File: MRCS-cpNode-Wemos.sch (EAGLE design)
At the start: 40 parts, among them CON1 3.5MM, CON2 3.5MM, J2 CONNECTOR-GROVE-4P-2.0-347013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, Q2 2n7002, Q3 2n7002, Q4 2n7002, Q5 2n7002, U3 NE555P, U4 MAX3465CPD

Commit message: 5.0
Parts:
- removed C4: 0.1uF, SPCoast:CC0805
- removed C6: .01uF, SPCoast:CC0805
- removed C7: .1uF, SPCoast:CC0805
- removed C8: .1uF, SPCoast:CC0603
- removed CON1, CON2: 3.5MM, SPCoast:CONNECTOR-M035MM-LOCK
- removed CON3, CON4: (no value), SPCoast:CONNECTOR-M025MM-LOCK
- removed D1: BAV-199, SPCoast:DIODE-BAV199
- removed R14: 1k0, SPCoast:R0805-RES
- removed RS485IN: (no value), SparkFun:M05PTH
- removed RS485OUT: (no value), SparkFun:M05LOCK
- removed TX: TX, SPCoast:LED0603-LED
- removed U3: NE555P, SparkFun:NE555P
- removed U4: MAX3465CPD, maxim:MAX3465CPD
- added CMRI-IO: (no value), SPCoast:CONNECTOR-M05LOCK_LONGPADS
- added Q1: 2n7002, SPCoast:MOSFET-N-BSS138-SOT23
- added R4: 10k, SPCoast:R0805-RES
- BOARD: device SPCoast:BOARD69X100 -> SPCoast:BOARD69X90
- R1: value (none) -> 10k; device SPCoast:RPTH-1/6W -> SPCoast:R0805-RES
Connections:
- removed net IN+: CON3.B, CON4.B, RS485IN.1, RS485OUT.1, U4.A
- removed net IN-: CON3.A, CON4.A, RS485IN.2, RS485OUT.2, U4.B
- removed net N$1: C4.1, D1.A, D1.AC, R1.1, U3.DIS, U3.TRE
- removed net N$29: R14.2, TX.A
- removed net N$38: C6.1, U3.CON
- removed net OUT+: CON1.3, CON2.3, RS485IN.3, RS485OUT.3, U4.Y
- removed net OUT-: CON1.2, CON2.2, RS485IN.4, RS485OUT.4, U4.Z
- removed net SHIELD: CON1.1, CON2.1, RS485IN.5, RS485OUT.5
- new net VCC: CMRI-IO.2
- net +3V3: now also Q1.G, R1.2
- net D5: now also Q1.S, R1.1
- net GND: now also CMRI-IO.1; no longer C4.2, C6.2, C7.2, C8.2, TX.C, U3.GND, U4.GND, U4.GND@1
- net RXH: now also CMRI-IO.4; no longer U4.RO
- net TXEN: now also CMRI-IO.5, Q1.D, R4.1; no longer R14.1, U3.OUT, U4.DE, U4.RE/
- net TXH: now also CMRI-IO.3; no longer D1.C, U3.TRI, U4.DI
- net VCCIO: now also R4.2; no longer C7.1, C8.1, R1.2, U3./RES, U3.VCC+, U4.VCC
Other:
- note removed: "115200 1000 0.1 uF"
- note removed: "19200 12000 0.1 uF"
- note removed: "38400 3000 0.1 uF"
- note removed: "57600 2000 0.1 uF"
- note removed: "9600 12000 0.1 uF"
- note removed: "AutoRTS"
- note removed: "AutoRTS Values"
- note removed: "BPS R1 C1"
- note removed: "IN+"
- note removed: "IN-"
- note removed: "MAX489"
- note removed: "OUT+"
- note removed: "OUT-"
- note removed: "RS-485 Interface"
- note removed: "Shield"
- note removed: "nc"
- moved on the sheet: R1

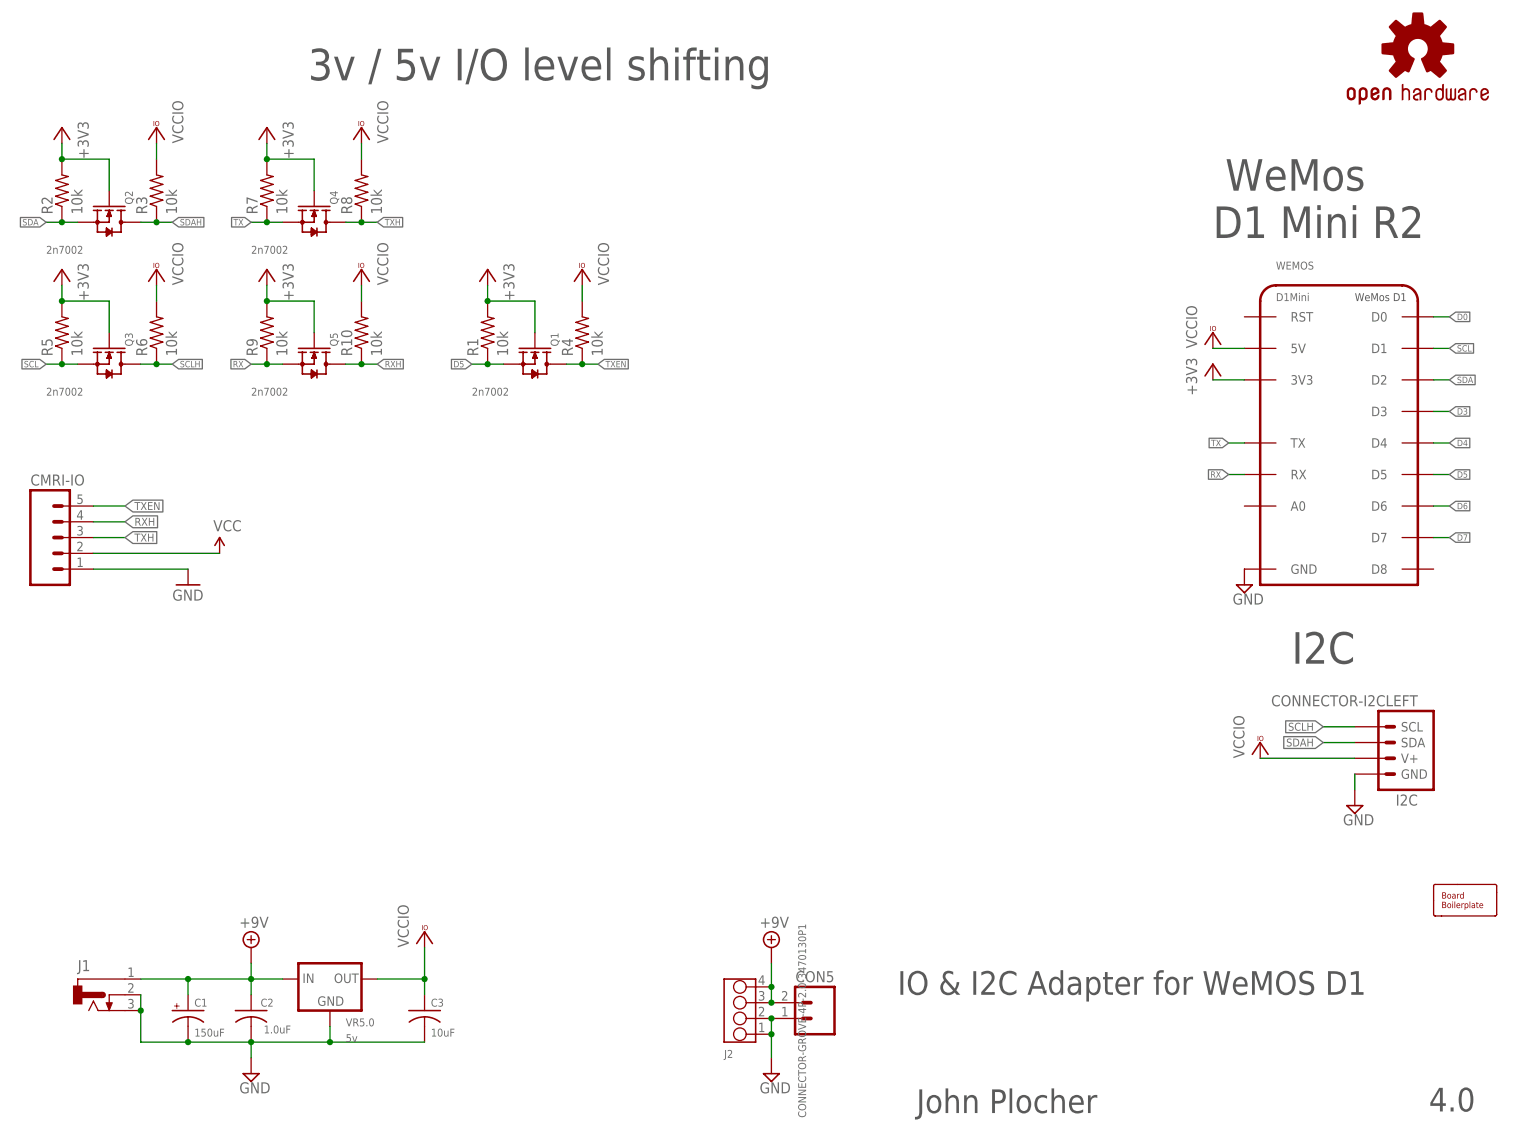
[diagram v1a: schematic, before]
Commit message: cleanup, DRC, ERC
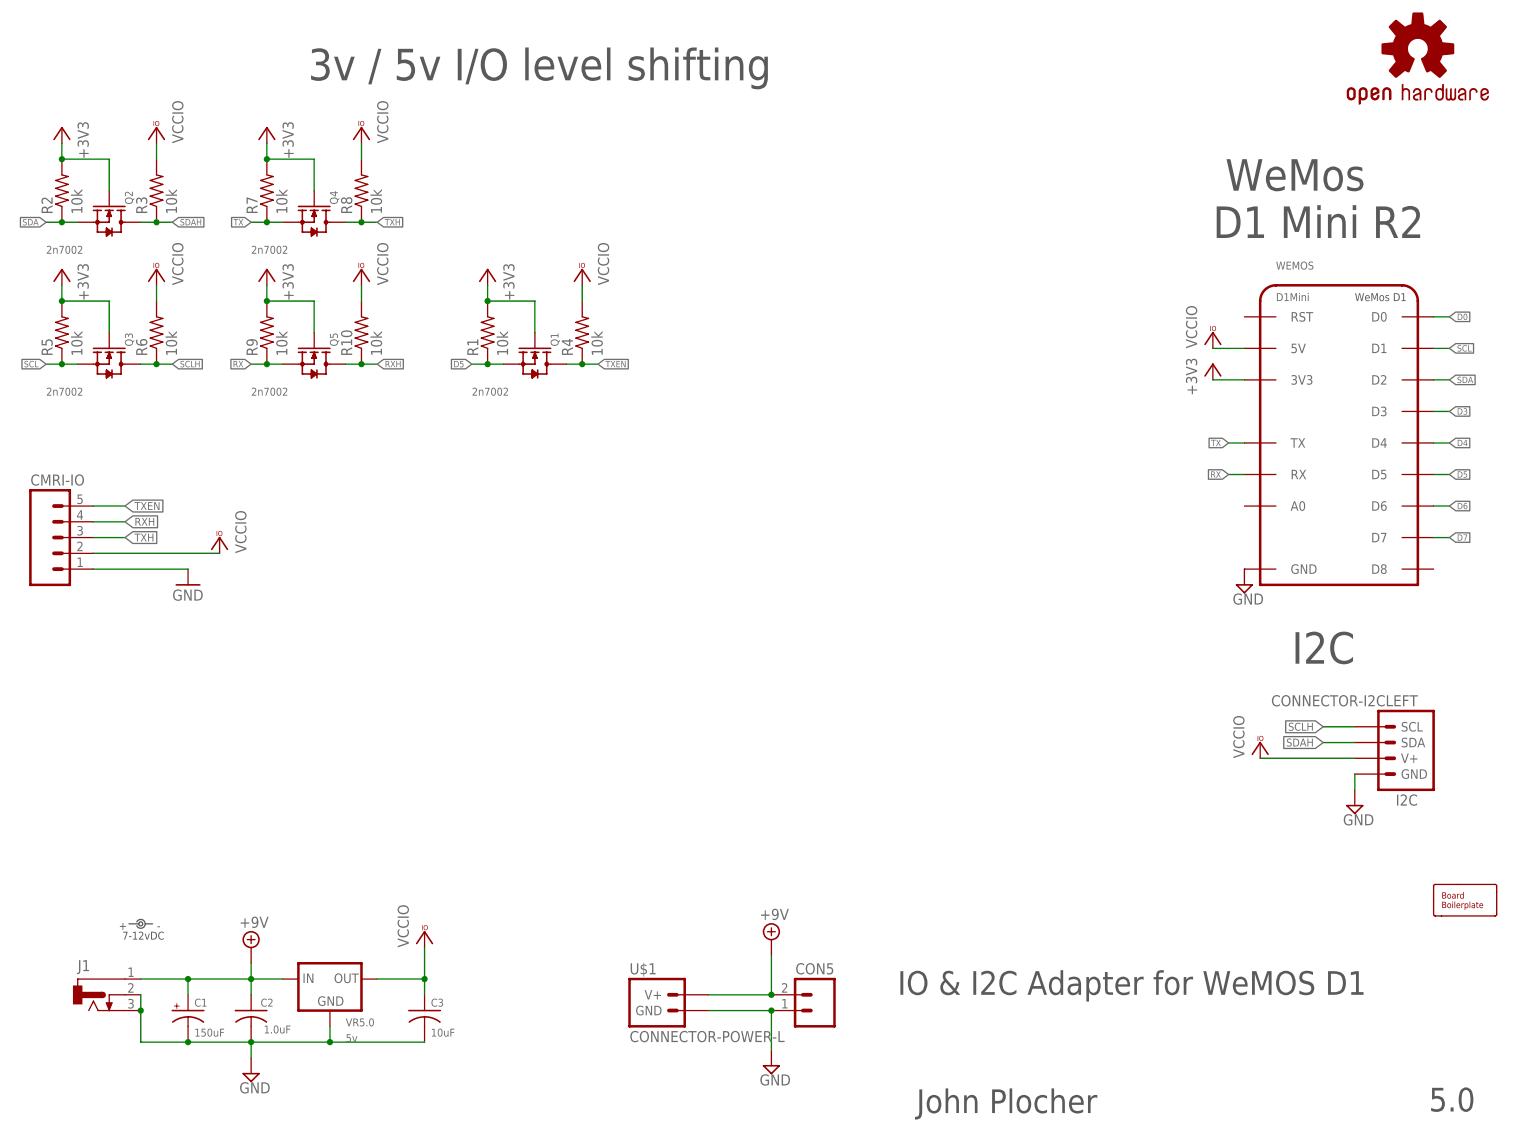
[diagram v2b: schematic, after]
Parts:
- removed J2: CONNECTOR-GROVE-4P-2.0-3470130P1, SPCoast:CONNECTOR-GROVE-4P-2.0-3470130P1
- added U$1: CONNECTOR-POWER-L, SPCoast:CONNECTOR-POWER-L
- BOARD: device SPCoast:BOARD69X90 -> SPCoast:BOARD69X80
- LABEL1: device SPCoast-minimal:POWER_LABEL -> SPCoast:DOC-POWER_LABEL
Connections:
- removed net VCC: CMRI-IO.2
- net +9V: now also U$1.V+; no longer J2.3, J2.4
- net GND: now also U$1.GND; no longer J2.1, J2.2
- net VCCIO: now also CMRI-IO.2
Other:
- note added: "5.0"
- note removed: "4.0"
- moved on the sheet: CON5

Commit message: added missing values
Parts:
- CMRI-IO: value (none) -> 0.100
- CON5: value (none) -> 3.5mm
- J1: value (none) -> 2.1mm
- U$1: value CONNECTOR-POWER-L -> I2C
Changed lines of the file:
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@@
 <grid distance="100" unitdist="mil" unit="mil" style="dots" multiple="1" display="yes" altdistance="50" altunitdist="mil" altunit="mil"/>
 <layers>
-<layer number="1" name="Top" color="4" fill="1" visible="yes" active="no"/>
-<layer number="2" name="Route2" color="1" fill="3" visible="yes" active="no"/>
-<layer number="3" name="Route3" color="4" fill="3" visible="yes" active="no"/>
-<layer number="4" name="Route4" color="1" fill="4" visible="yes" active="no"/>
-<layer number="5" name="Route5" color="4" fill="4" visible="yes" active="no"/>
-<layer number="6" name="Route6" color="1" fill="8" visible="yes" active="no"/>
-<layer number="7" name="Route7" color="4" fill="8" visible="yes" active="no"/>
-<layer number="8" name="Route8" color="1" fill="2" visible="yes" active="no"/>
-<layer number="9" name="Route9" color="4" fill="2" visible="yes" active="no"/>
-<layer number="10" name="Route10" color="1" fill="7" visible="yes" active="no"/>
-<layer number="11" name="Route11" color="4" fill="7" visible="yes" active="no"/>
-<layer number="12" name="Route12" color="1" fill="5" visible="yes" active="no"/>
-<layer number="13" name="Route13" color="4" fill="5" visible="yes" active="no"/>
-<layer number="14" name="Route14" color="1" fill="6" visible="yes" active="no"/>
-<layer number="15" name="Route15" color="4" fill="6" visible="yes" active="no"/>
-<layer number="16" name="Bottom" color="2" fill="1" visible="yes" active="no"/>
-<layer number="17" name="Pads" color="23" fill="1" visible="yes" active="no"/>
-<layer number="18" name="Vias" color="29" fill="1" visible="yes" active="no"/>
-<layer number="19" name="Unrouted" color="36" fill="1" visible="yes" active="no"/>
-<layer number="20" name="Dimension" color="15" fill="1" visible="yes" active="no"/>
-<layer number="21" name="tPlace" color="36" fill="1" visible="yes" active="no"/>
-<layer number="22" name="bPlace" color="17" fill="1" visible="yes" active="no"/>
-<layer number="23" name="tOrigins" color="30" fill="1" visible="yes" active="no"/>
-<layer number="24" name="bOrigins" color="15" fill="1" visible="yes" active="no"/>
-<layer number="25" name="tNames" color="63" fill="1" visible="yes" active="no"/>
-<layer number="26" name="bNames" color="34" fill="1" visible="yes" active="no"/>
-<layer number="27" name="tValues" color="56" fill="1" visible="yes" active="no"/>
-<layer number="28" name="bValues" color="7" fill="1" visible="yes" active="no"/>
+<layer number="1" name="Top" color="4" fill="1" visible="no" active="no"/>
+<layer number="2" name="Route2" color="1" fill="3" visible="no" active="no"/>
+<layer number="3" name="Route3" color="4" fill="3" visible="no" active="no"/>
+<layer number="4" name="Route4" color="1" fill="4" visible="no" active="no"/>
+<layer number="5" name="Route5" color="4" fill="4" visible="no" active="no"/>
+<layer number="6" name="Route6" color="1" fill="8" visible="no" active="no"/>
+<layer number="7" name="Route7" color="4" fill="8" visible="no" active="no"/>
+<layer number="8" name="Route8" color="1" fill="2" visible="no" active="no"/>
+<layer number="9" name="Route9" color="4" fill="2" visible="no" active="no"/>
+<layer number="10" name="Route10" color="1" fill="7" visible="no" active="no"/>
+<layer number="11" name="Route11" color="4" fill="7" visible="no" active="no"/>
+<layer number="12" name="Route12" color="1" fill="5" visible="no" active="no"/>
+<layer number="13" name="Route13" color="4" fill="5" visible="no" active="no"/>
+<layer number="14" name="Route14" color="1" fill="6" visible="no" active="no"/>
+<layer number="15" name="Route15" color="4" fill="6" visible="no" active="no"/>
+<layer number="16" name="Bottom" color="2" fill="1" visible="no" active="no"/>
+<layer number="17" name="Pads" color="23" fill="1" visible="no" active="no"/>
+<layer number="18" name="Vias" color="29" fill="1" visible="no" active="no"/>
+<layer number="19" name="Unrouted" color="36" fill="1" visible="no" active="no"/>
+<layer number="20" name="Dimension" color="15" fill="1" visible="no" active="no"/>
+<layer number="21" name="tPlace" color="36" fill="1" visible="no" active="no"/>
+<layer number="22" name="bPlace" color="17" fill="1" visible="no" active="no"/>
+<layer number="23" name="tOrigins" color="30" fill="1" visible="no" active="no"/>
+<layer number="24" name="bOrigins" color="15" fill="1" visible="no" active="no"/>
+<layer number="25" name="tNames" color="63" fill="1" visible="no" active="no"/>
+<layer number="26" name="bNames" color="34" fill="1" visible="no" active="no"/>
+<layer number="27" name="tValues" color="56" fill="1" visible="no" active="no"/>
+<layer number="28" name="bValues" color="7" fill="1" visible="no" active="no"/>
 <layer number="29" name="tStop" color="7" fill="3" visible="no" active="no"/>
 <layer number="30" name="bStop" color="7" fill="6" visible="no" active="no"/>
@@
 <layer number="35" name="tGlue" color="7" fill="4" visible="no" active="no"/>
 <layer number="36" name="bGlue" color="7" fill="5" visible="no" active="no"/>
-<layer number="37" name="tTest" color="7" fill="1" visible="yes" active="no"/>
-<layer number="38" name="bTest" color="7" fill="1" visible="yes" active="no"/>
+<layer number="37" name="tTest" color="7" fill="1" visible="no" active="no"/>
+<layer number="38" name="bTest" color="7" fill="1" visible="no" active="no"/>
 <layer number="39" name="tKeepout" color="4" fill="11" visible="no" active="no"/>
 <layer number="40" name="bKeepout" color="3" fill="11" visible="no" active="no"/>
@@
 <layer number="44" name="Drills" color="16" fill="1" visible="no" active="no"/>
 <layer number="45" name="Holes" color="35" fill="1" visible="no" active="no"/>
-<layer number="46" name="Milling" color="35" fill="1" visible="yes" active="no"/>
-<layer number="47" name="Measures" color="21" fill="1" visible="yes" active="no"/>
-<layer number="48" name="Document" color="24" fill="1" visible="yes" active="no"/>
-<layer number="49" name="Reference" color="48" fill="1" visible="yes" active="no"/>
-<layer number="50" name="dxf" color="7" fill="1" visible="yes" active="no"/>
-<layer number="51" name="tDocu" color="24" fill="1" visible="yes" active="no"/>
-<layer number="52" name="bDocu" color="7" fill="1" visible="yes" active="no"/>
-<layer number="53" name="tGND_GNDA" color="7" fill="9" visible="yes" active="no"/>
-<layer number="54" name="bGND_GNDA" color="1" fill="9" visible="yes" active="no"/>
-<layer number="56" name="wert" color="7" fill="1" visible="yes" active="no"/>
-<layer number="57" name="tCAD" color="7" fill="1" visible="yes" active="no"/>
-<layer number="59" name="tCarbon" color="7" fill="1" visible="yes" active="no"/>
-<layer number="60" name="bCarbon" color="7" fill="1" visible="yes" active="no"/>
+<layer number="46" name="Milling" color="35" fill="1" visible="no" active="no"/>
+<layer number="47" name="Measures" color="21" fill="1" visible="no" active="no"/>
+<layer number="48" name="Document" color="24" fill="1" visible="no" active="no"/>
+<layer number="49" name="Reference" color="48" fill="1" visible="no" active="no"/>
+<layer number="50" name="dxf" color="7" fill="1" visible="no" active="no"/>
+<layer number="51" name="tDocu" color="24" fill="1" visible="no" active="no"/>
+<layer number="52" name="bDocu" color="7" fill="1" visible="no" active="no"/>
+<layer number="53" name="tGND_GNDA" color="7" fill="9" visible="no" active="no"/>
+<layer number="54" name="bGND_GNDA" color="1" fill="9" visible="no" active="no"/>
+<layer number="56" name="wert" color="7" fill="1" visible="no" active="no"/>
+<layer number="57" name="tCAD" color="7" fill="1" visible="no" active="no"/>
+<layer number="59" name="tCarbon" color="7" fill="1" visible="no" active="no"/>
+<layer number="60" name="bCarbon" color="7" fill="1" visible="no" active="no"/>
 <layer number="90" name="Modules" color="5" fill="1" visible="no" active="no"/>
 <layer number="91" name="Nets" color="2" fill="1" visible="yes" active="yes"/>
@@
 <part name="V5" library="supply2" deviceset="GND" device=""/>
 <part name="SUPPLY1" library="supply2" deviceset="+9V" device=""/>
-<part name="J1" library="SPCoast" deviceset="CONNECTOR-DC-POWER" device="-RA"/>
+<part name="J1" library="SPCoast" deviceset="CONNECTOR-DC-POWER" device="-RA" value="2.1mm"/>
 <part name="LABEL1" library="SPCoast" deviceset="DOC-POWER_LABEL" device="" value="7-12vDC"/>
 <part name="VCC12" library="supply1" deviceset="VCCIO" device=""/>
@@
 <part name="3V6" library="supply1" deviceset="+3V3" device=""/>
 <part name="VCC9" library="supply1" deviceset="VCCIO" device=""/>
-<part name="CON5" library="SPCoast" deviceset="CONNECTOR-M02" device="3.5MM-LOCK"/>
-<part name="CMRI-IO" library="SPCoast" deviceset="CONNECTOR-M05" device="LOCK_LONGPADS"/>
+<part name="CON5" library="SPCoast" deviceset="CONNECTOR-M02" device="3.5MM-LOCK" value="3.5mm"/>
+<part name="CMRI-IO" library="SPCoast" deviceset="CONNECTOR-M05" device="LOCK_LONGPADS" value="0.100"/>
 <part name="GND1" library="SparkFun" deviceset="GND" device=""/>
 <part name="Q1" library="SPCoast" deviceset="MOSFET-N-*-?" device="SOT23" technology="BSS138" value="2n7002"/>
@@
 <part name="3V2" library="supply1" deviceset="+3V3" device=""/>
 <part name="VCC2" library="supply1" deviceset="VCCIO" device=""/>
-<part name="U$1" library="SPCoast" deviceset="CONNECTOR-POWER" device="-L"/>
+<part name="U$1" library="SPCoast" deviceset="CONNECTOR-POWER" device="-L" value="I2C"/>
 <part name="VCC3" library="supply1" deviceset="VCCIO" device=""/>
 </parts>
